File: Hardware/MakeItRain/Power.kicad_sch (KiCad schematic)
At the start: 5 parts, among them J5 Conn_01x03, P1 Screw_Terminal_01x02, Q13 IRF9Z34NPBF, U2 178.6165.0001

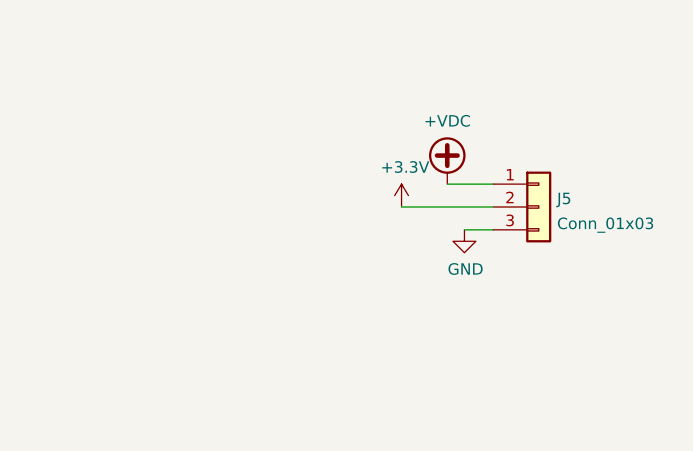
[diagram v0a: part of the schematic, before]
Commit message: wip for adding RTC
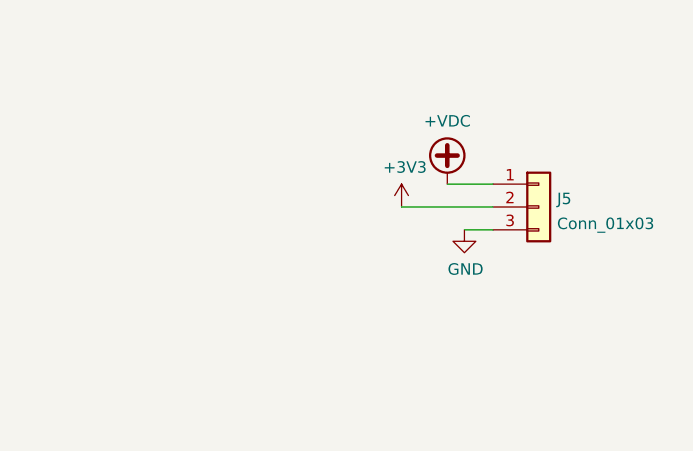
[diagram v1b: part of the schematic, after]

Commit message: wip
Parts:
- R21: footprint Resistor_THT:R_Axial_DIN0207_L6.3mm_D2.5mm_P2.54mm_Vertical -> Resistor_SMD:R_1206_3216Metric_Pad1.30x1.75mm_HandSolder
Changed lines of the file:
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@@
 			)
 		)
-		(property "Footprint" "Resistor_THT:R_Axial_DIN0207_L6.3mm_D2.5mm_P2.54mm_Vertical"
+		(property "Footprint" "Resistor_SMD:R_1206_3216Metric_Pad1.30x1.75mm_HandSolder"
 			(at 62.992 73.66 90)
 			(effects
